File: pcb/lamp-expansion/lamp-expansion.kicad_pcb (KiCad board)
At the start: 2 copper layers, 53.3 x 46.2 mm, 83 parts, among them IC1 PAM2421, IC2 MCP73811, IC3 AP2411_ep, IC6 LM1117_5.0, IC7 FT230X_SOP, IC9 CC3000, J1 MICROUSB, J2 DCIN, J3 SERIAL, J4 5PIN_INPUT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

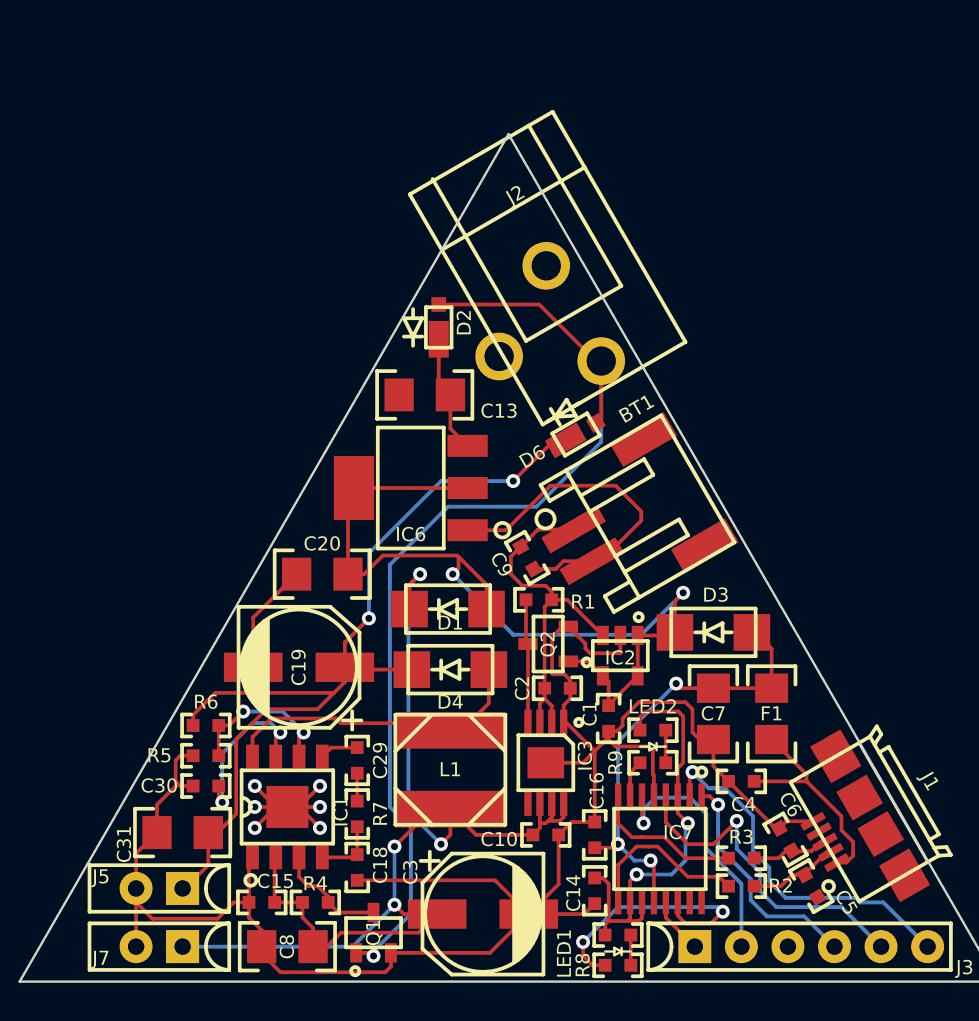
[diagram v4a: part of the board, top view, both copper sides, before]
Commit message: a little more room fort activities
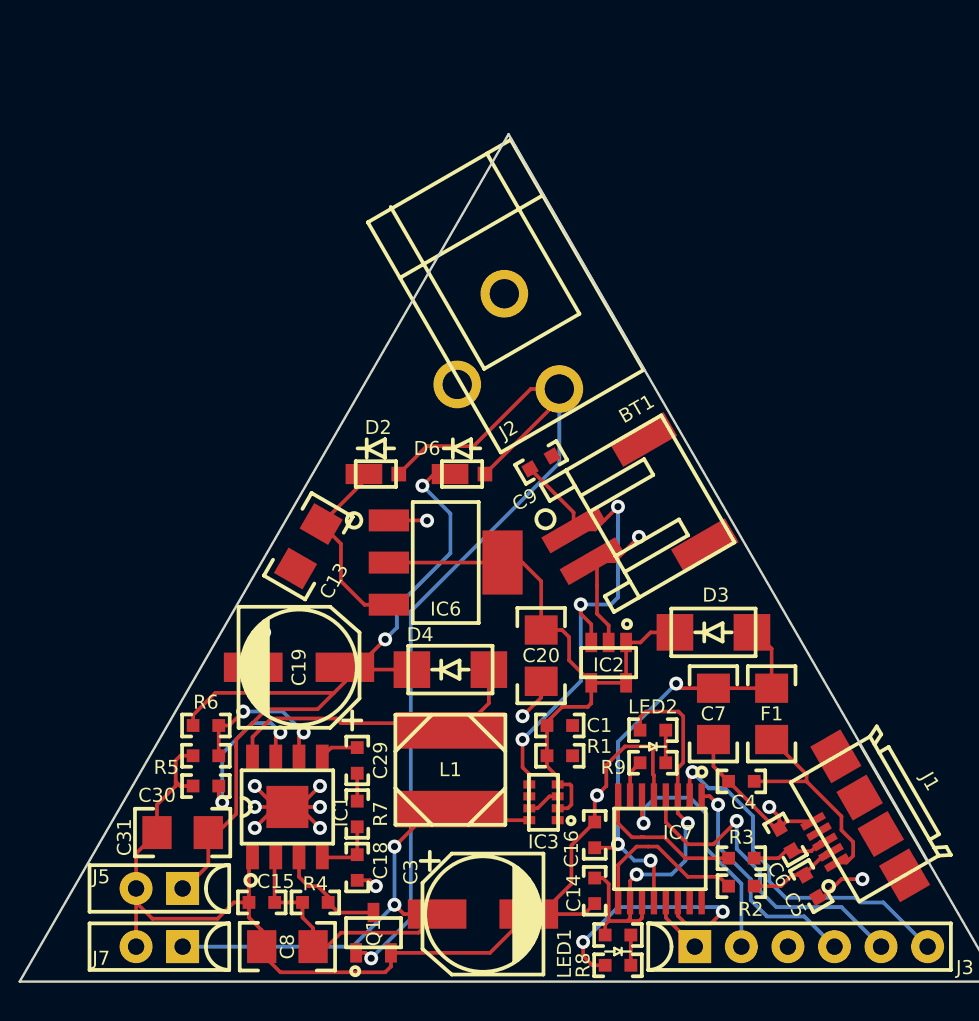
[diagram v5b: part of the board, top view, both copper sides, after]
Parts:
- removed C10, C2: 0.1uF, passive-smd:0603(1608m)
- removed D1: 3A, diode:DO-214AC
- removed Q2: 2N7002, sot:SOT23
- IC3: value AP2411_ep -> NTHD3101F; footprint sop:MSOP8_ep -> sot:CHIPFET-1206-8
- R1: value 10kΩ -> 100kΩ
- moved C20 12.7 mm to (79.2, 109.2), turned to 270 degrees
- moved C13 10.4 mm to (66.5, 103.3), turned to 240 degrees
- moved D2 8.70 mm to (70.2, 99.3), turned to 0 degrees
- moved R1 8.59 mm to (80.3, 114.7)
- moved D6 6.59 mm to (74.9, 99.3), turned to 0 degrees
- moved C9 5.26 mm to (79.2, 98.7), turned to 30 degrees
- moved IC6 4.49 mm to (74.0, 104.1), turned to 0 degrees
- moved J2 2.75 mm to (78.7, 92.1)
- moved C1 2.69 mm to (80.3, 113.0), turned to 0 degrees
- moved IC3 2.16 mm to (79.4, 117.2), turned to 180 degrees
- moved IC2 0.74 mm to (82.9, 109.6)
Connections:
- BT1 pad 1: +BATT -> Net-(BT1-Pad1)
- C9 pad 1: +BATT -> Net-(BT1-Pad1)
- IC2 pad 3: +BATT -> Net-(BT1-Pad1)
- IC3 pad 1: GND -> +5V
- IC3 pad 2: +BATT -> +5V
- IC3 pad 3: +BATT -> /VSUP
- IC3 pad 4: Net-(IC3-Pad4) -> +5V
- IC3 pad 5: Net-(IC3-Pad5) -> Net-(BT1-Pad1)
- IC3 pad 6: /VSUP -> Net-(BT1-Pad1)
- R1 pad 1: +BATT -> GND
- R1 pad 2: Net-(IC3-Pad4) -> +5V
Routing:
- net GND: track 150.1 -> 109.5 mm, vias 6 -> 14
- net Net-(BT1-Pad1): track 0.00 -> 28.6 mm, vias 0 -> 3
- net /VSUP: track 67.4 -> 46.7 mm, vias 4 -> 2
- net +BATT: track 20.1 -> 0.00 mm
- net +5V: track 49.9 -> 34.2 mm, vias 2 -> 0
- net Net-(IC3-Pad4): track 6.74 -> 0.00 mm
- net /V_LED: track 50.3 -> 45.4 mm
- net Net-(C13-Pad1): track 6.47 -> 10.4 mm
- net /DC_IN: track 56.1 -> 53.3 mm

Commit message: continue layout work
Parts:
- moved VR1 111.8 mm to (228.6, 91.4)
- moved VR2 109.0 mm to (228.6, 119.4)
- moved VR3 107.4 mm to (228.6, 104.1)
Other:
- board size 53.3 x 46.2 mm -> 139.7 x 46.2 mm

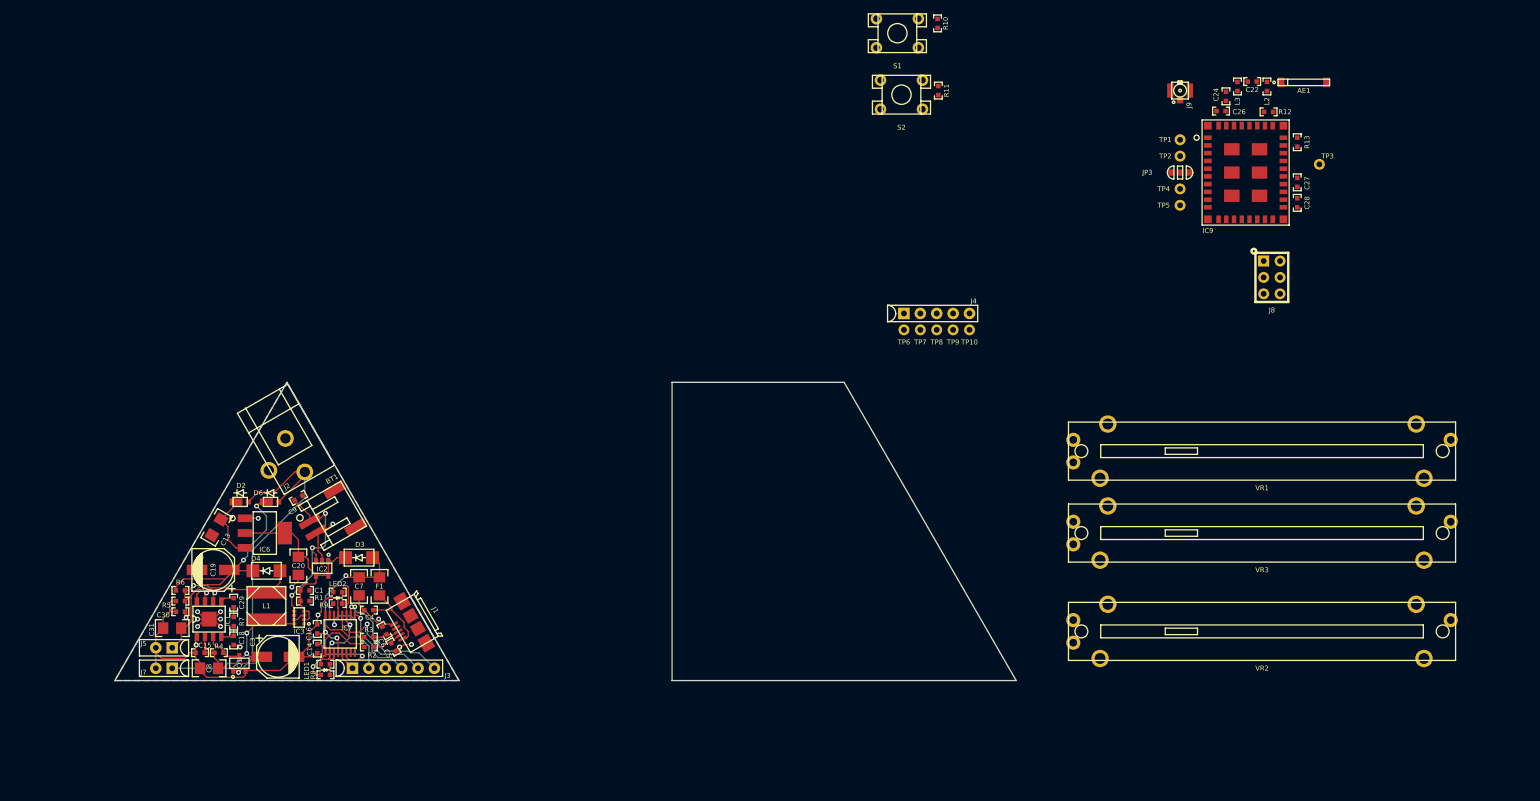
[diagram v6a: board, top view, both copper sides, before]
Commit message: layout and schematic refinements
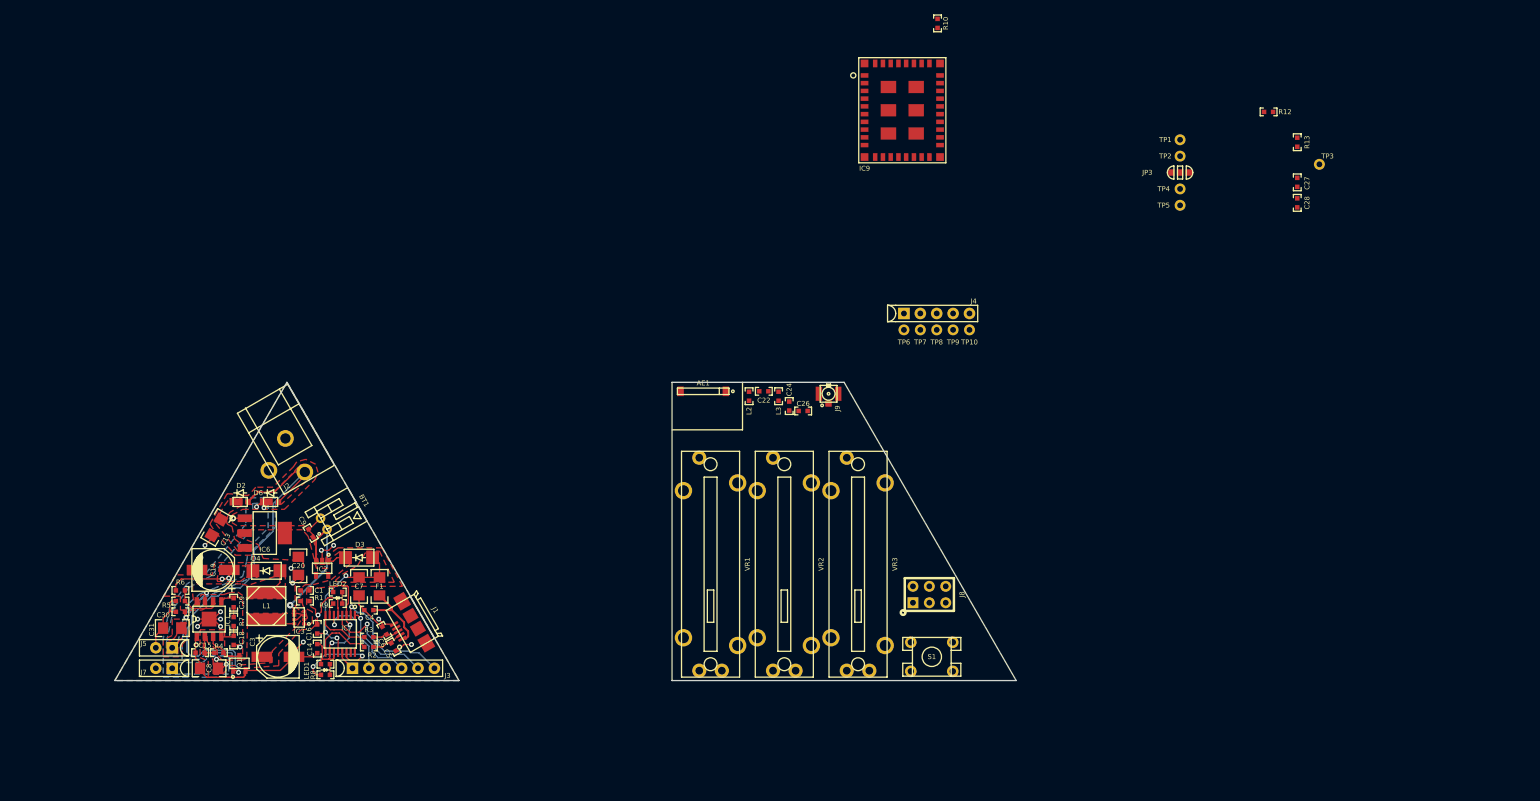
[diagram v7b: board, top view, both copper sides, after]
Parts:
- removed R11: 10kΩ, passive-smd:0603(1608m)
- removed S2: SPST, switch:SPST-4-PIN_6mm_thru
- BT1: footprint connect-sm:JST-S2B-PH-SM4-TB_right-angle-jack -> connect-thru:JST-S2B-PH-K_right-angle-jack
- VR1, VR2, VR3: footprint bourns:BOURNS-PTA4543_slide-pot -> bourns:BOURNS-PTA2043_20mm-slide-pot
- moved AE1 104.7 mm to (142.0, 82.2), turned to 180 degrees
- moved S1 96.8 mm to (177.4, 123.3), turned to 180 degrees
- moved L2 93.5 mm to (149.1, 82.9)
- moved C22 89.6 mm to (151.4, 82.2), turned to 0 degrees
- moved VR1 87.2 mm to (143.1, 109.0), turned to 90 degrees
- moved L3 85.8 mm to (153.7, 82.9)
- moved C24 83.0 mm to (155.3, 84.5)
- moved C26 79.7 mm to (157.5, 85.2), turned to 0 degrees
- moved VR2 74.8 mm to (154.6, 109.0), turned to 90 degrees
- moved J8 72.3 mm to (177.0, 113.7), turned to 90 degrees
- moved J9 71.9 mm to (161.4, 82.5)
- moved VR3 62.8 mm to (166.0, 109.0), turned to 90 degrees
- moved IC9 54.1 mm to (172.8, 38.6)
- moved C9 5.78 mm to (81.2, 104.1), turned to 120 degrees
- moved BT1 1.02 mm to (85.1, 101.6), turned to 120 degrees
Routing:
- net +5V: track 34.2 -> 4.04 mm
- net /V_LED: track 45.4 -> 16.9 mm, vias 2 -> 4
- net /VSUP: track 46.7 -> 18.9 mm
- net GND: track 109.5 -> 95.2 mm, vias 14 -> 17
- net /DC_IN: track 53.3 -> 66.8 mm
- net Net-(D4-Pad2): track 17.1 -> 5.10 mm
- net Net-(C13-Pad1): track 10.4 -> 0.39 mm
- net Net-(BT1-Pad1): track 28.6 -> 22.3 mm, vias 3 -> 1
- net Net-(C30-Pad1): track 9.44 -> 7.83 mm
- net Net-(IC1-Pad6): track 8.49 -> 7.45 mm, vias 2 -> 0
- added copper zone on F.Cu, net +5V
- added copper zone on F.Cu, net /DC_IN
- added copper zone on B.Cu, net /VSUP
- added copper zone on F.Cu, net /VSUP
- added copper zone on B.Cu, net /V_LED
- added copper zone on F.Cu, net /V_LED
- added copper zone on F.Cu, net /V_USB
- added copper zone on F.Cu, net Net-(C13-Pad1)
- added copper zone on F.Cu, net Net-(D4-Pad2)
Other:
- net class BATIN added: clearance 0.254, trace_width 0.3048, via_dia 1.016, via_drill 0.635
- net class USBIN added: clearance 0.2286, trace_width 0.3048, via_dia 0.762, via_drill 0.381

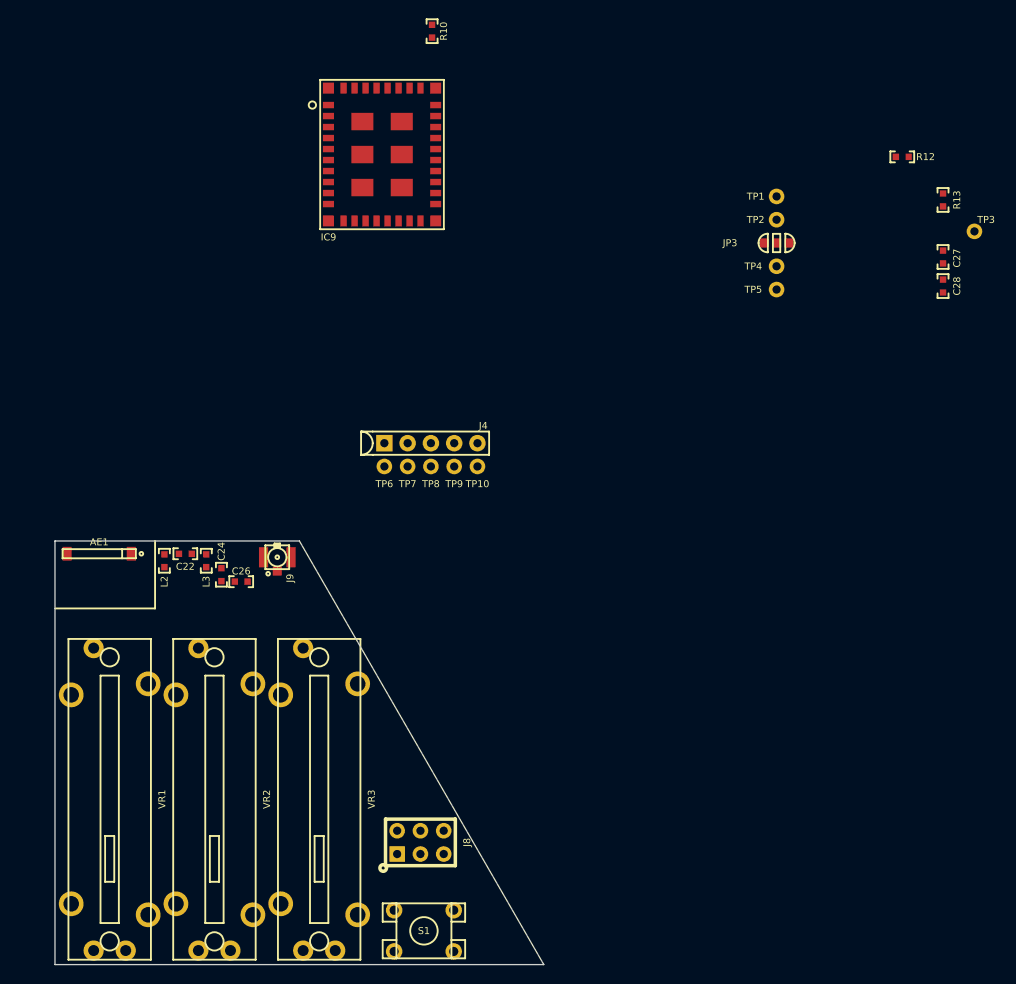
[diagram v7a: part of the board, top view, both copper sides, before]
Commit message: still need to match nets up between main and expansion
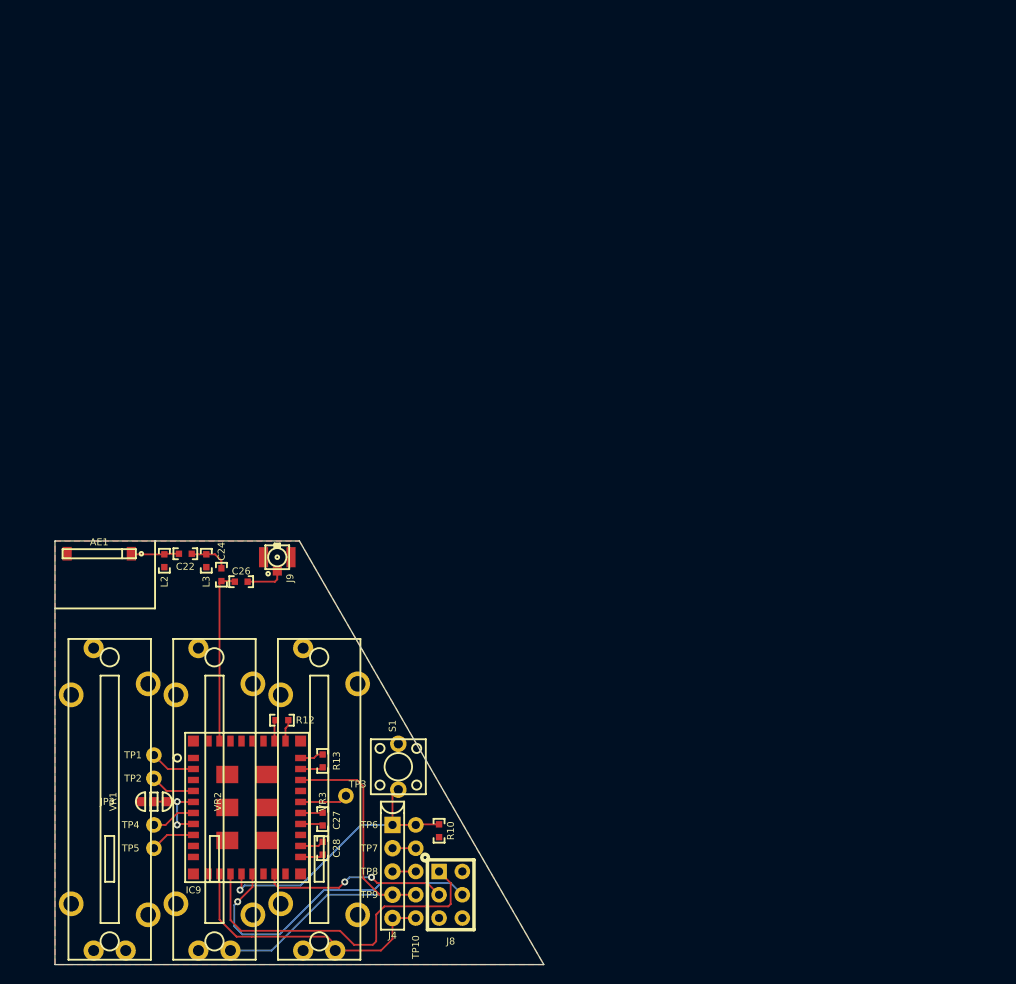
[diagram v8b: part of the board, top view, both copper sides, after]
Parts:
- S1: footprint switch:SPST-4-PIN_6mm_thru -> switch:SPST-2-PIN_6mm_thru
- moved TP3 92.2 mm to (168.9, 108.6)
- moved R12 91.4 mm to (161.9, 100.3)
- moved C27 91.3 mm to (166.4, 111.1)
- moved C28 91.3 mm to (166.4, 114.3)
- moved JP3 91.3 mm to (148.0, 109.2)
- moved TP1 91.3 mm to (148.0, 104.1)
- moved TP2 91.3 mm to (148.0, 106.7)
- moved TP4 91.3 mm to (148.0, 111.8)
- moved TP5 91.3 mm to (148.0, 114.3)
- moved R13 91.3 mm to (166.4, 104.8)
- moved R10 87.3 mm to (179.1, 112.4)
- moved IC9 72.8 mm to (158.1, 109.9)
- moved TP10 49.7 mm to (176.5, 121.9)
- moved J4 46.9 mm to (174.0, 116.8), turned to 270 degrees
- moved TP9 46.9 mm to (176.5, 119.4)
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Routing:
- net /CC_EN: track 0.00 -> 43.8 mm
- net /CC_MISO: track 0.00 -> 37.8 mm
- net /CC_MOSI: track 0.00 -> 34.6 mm, vias 0 -> 1
- net /CC_SEL: track 0.00 -> 31.0 mm
- net /CC_IRQ: track 0.00 -> 30.6 mm, vias 0 -> 1
- net /CC_SCK: track 0.00 -> 20.5 mm, vias 0 -> 2
- net Net-(C24-Pad1): track 0.00 -> 19.0 mm
- net Net-(IC9-Pad5): track 0.00 -> 8.68 mm, vias 0 -> 2
- net Net-(AE1-Pad1): track 0.00 -> 5.25 mm
- net Net-(IC9-Pad24): track 0.00 -> 5.22 mm
- net GND: track 95.2 -> 100.3 mm
- net Net-(IC9-Pad2): track 0.00 -> 4.94 mm
- net VCC: track 0.00 -> 4.93 mm
- net Net-(IC9-Pad8): track 0.00 -> 4.91 mm
- net Net-(IC9-Pad4): track 0.00 -> 4.88 mm
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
